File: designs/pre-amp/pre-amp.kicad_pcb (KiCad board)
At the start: 4 copper layers, 56.4 x 24.9 mm, 28 parts, among them J1 Conn_Coaxial, J2 Conn_01x03, J3 Conn_Coaxial, U1 AD8429, U2 OP211

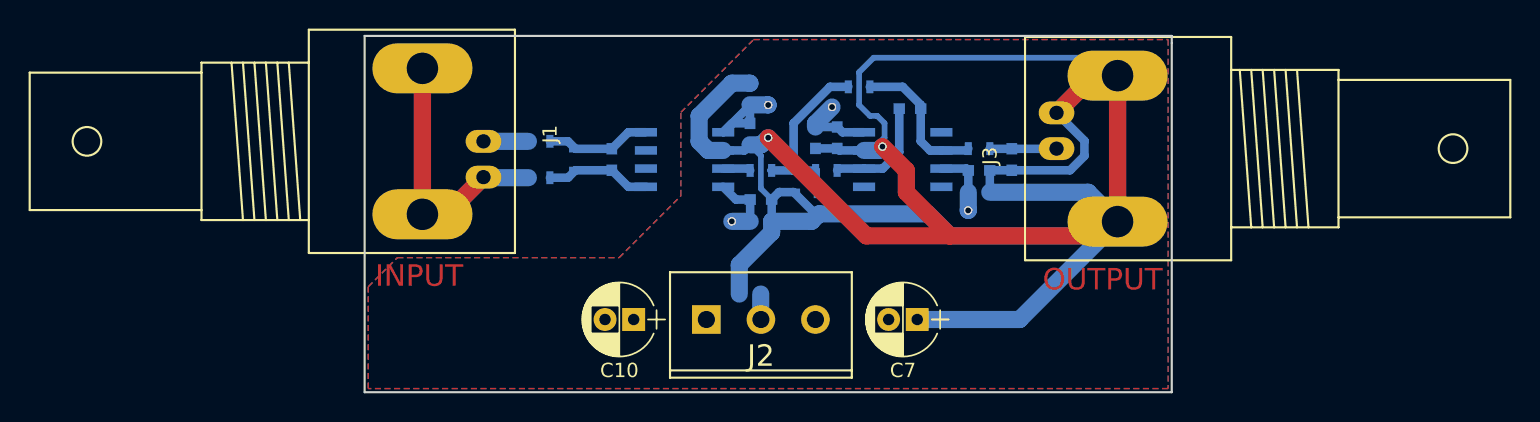
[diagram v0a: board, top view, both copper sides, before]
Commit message: [designs/pre-amp] new layout
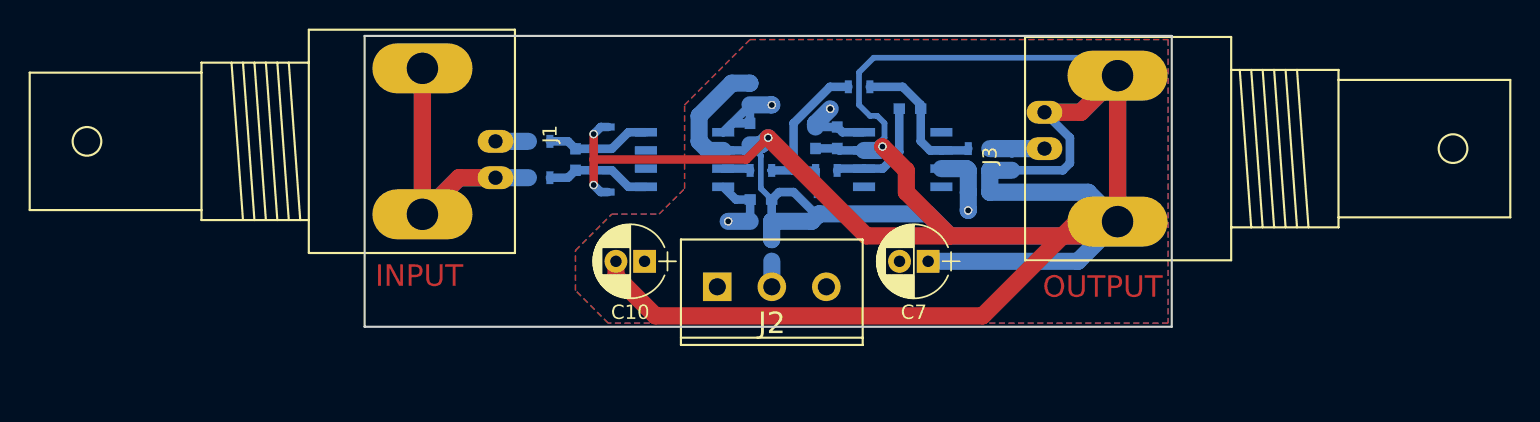
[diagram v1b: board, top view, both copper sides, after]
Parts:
- C14: value C -> 0
- J1, J3: footprint Connectors_TE-Connectivity:BNC_Socket_TYCO-AMP_LargePads -> Connectors2:BNC_Socket_Right-Angle_LargePads
- R4: value 20k -> 100k
- R8: value R -> 0
- R9: value R -> 100k
- moved R9 13.3 mm to (70.9, 64.5), turned to 270 degrees
- moved C10 4.13 mm to (73.4, 73.2)
- moved C7 4.13 mm to (93.2, 73.2)
- moved R3 3.41 mm to (82.3, 72.4), turned to 90 degrees
- moved R4 2.75 mm to (70.9, 67.6)
- moved C2 2.54 mm to (68.6, 66.0)
- moved J2 2.41 mm to (82.3, 74.9)
- moved J1 0.76 mm to (57.9, 64.8)
- moved J3 0.76 mm to (106.4, 65.3)
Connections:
- R4 pad 1: Net-(C2-Pad2) -> Net-(C2-Pad1)
- R4 pad 2: Net-(C2-Pad1) -> GND
- R9 pad 2: Net-(C12-Pad1) -> Net-(C2-Pad2)
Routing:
- net +15V: track 62.7 -> 52.7 mm
- net GND: track 238.4 -> 245.2 mm, vias 2 -> 4
- net -15V: track 52.9 -> 47.1 mm
- net Net-(J2-Pad2): track 3.91 -> 1.79 mm
- net Net-(J1-Pad1): track 3.14 -> 2.30 mm
- net Net-(C14-Pad1): track 4.67 -> 3.87 mm
- net Net-(J1-Pad2): track 34.2 -> 35.0 mm
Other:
- board size 56.4 x 24.9 mm -> 56.4 x 20.3 mm

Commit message: [designs/pre-amp] flip input and tweak connection near the edges
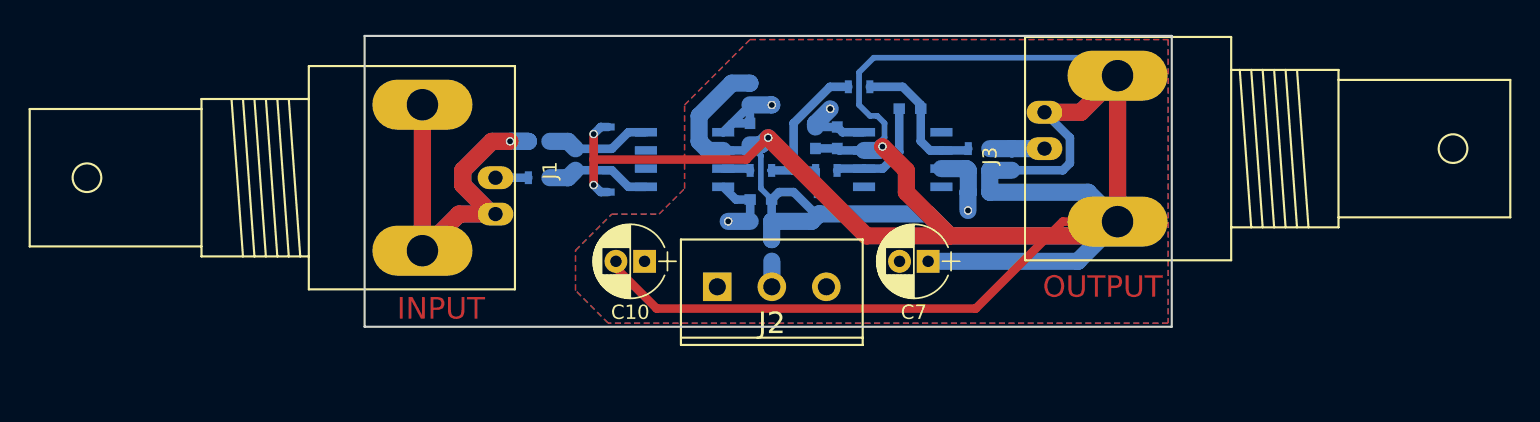
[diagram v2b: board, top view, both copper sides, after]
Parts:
- moved J1 2.54 mm to (57.9, 67.3)
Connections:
- R1 pad 2: Net-(J1-Pad2) -> Net-(J1-Pad1)
- R2 pad 2: Net-(J1-Pad1) -> Net-(J1-Pad2)
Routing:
- net +15V: track 52.7 -> 184.7 mm
- net Net-(J1-Pad2): track 35.0 -> 68.4 mm, vias 0 -> 1
- net GND: track 245.2 -> 247.3 mm
- net Net-(C2-Pad2): track 7.40 -> 9.41 mm
- net Net-(C2-Pad1): track 7.40 -> 9.41 mm

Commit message: [designs/pre-amp] move label location and update values
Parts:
- C2: value 0.02u -> 2200p
- R1, R2: value 1k -> 1.01k
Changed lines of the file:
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@@
     (links 55)
     (no_connects 0)
-    (area 30.174519 55.43586 134.163481 79.269001)
+    (area 53.772999 57.328999 110.311001 77.799001)
     (thickness 1.6)
-    (drawings 6)
+    (drawings 8)
     (tracks 252)
     (zones 0)
@@
     (nets 19)
   )
-  (page A4)
+  (page USLetter)
   (layers
     (0 F.Cu signal)
@@
   )
   (setup
-    (last_trace_width 1.2)
+    (last_trace_width 0.6)
     (user_trace_width 0.4)
     (user_trace_width 1.2)
@@
     (tags "capacitor 0603")
     (attr smd)
-    (fp_text reference C1 (at 0 1.5 270) (layer B.SilkS)
-      (effects (font (size 1 1) (thickness 0.15)) (justify mirror))
+    (fp_text reference C1 (at -0.182 -1.208 270) (layer B.SilkS)
+      (effects (font (size 0.762 0.762) (thickness 0.127)) (justify mirror))
     )
     (fp_text value 0.1u (at 0 -1.5 270) (layer B.Fab)
@@
     (tags "capacitor 0603")
     (attr smd)
-    (fp_text reference C2 (at 0 1.5 90) (layer B.SilkS)
-      (effects (font (size 1 1) (thickness 0.15)) (justify mirror))
-    )
-    (fp_text value 0.02u (at 0 -1.5 90) (layer B.Fab)
+    (fp_text reference C2 (at -2.38 0.08 90) (layer B.SilkS)
+      (effects (font (size 1 1) (thickness 0.15)) (justify mirror))
+    )
+    (fp_text value 2200p (at 0 -1.5 90) (layer B.Fab)
       (effects (font (size 1 1) (thickness 0.15)) (justify mirror))
     )
@@
     (tags "capacitor 0603")
     (attr smd)
-    (fp_text reference C3 (at 0 1.5 90) (layer B.SilkS)
+    (fp_text reference C3 (at 2.338 0.098 90) (layer B.SilkS)
       (effects (font (size 1 1) (thickness 0.15)) (justify mirror))
     )
@@
     (tags "capacitor 0603")
     (attr smd)
-    (fp_text reference C4 (at 0 1.5) (layer B.SilkS)
+    (fp_text reference C4 (at -2.424 0.726) (layer B.SilkS)
       (effects (font (size 1 1) (thickness 0.15)) (justify mirror))
     )
@@
     (tags "capacitor 0603")
     (attr smd)
-    (fp_text reference C6 (at 0 1.5 270) (layer B.SilkS)
-      (effects (font (size 1 1) (thickness 0.15)) (justify mirror))
+    (fp_text reference C6 (at -1.826 -0.032 360) (layer B.SilkS)
+      (effects (font (size 0.762 0.762) (thickness 0.127)) (justify mirror))
     )
     (fp_text value 0.1u (at 0 -1.5 270) (layer B.Fab)
@@
     (tags "capacitor 0603")
     (attr smd)
-    (fp_text reference C8 (at 0 1.5 270) (layer B.SilkS)
-      (effects (font (size 1 1) (thickness 0.15)) (justify mirror))
+    (fp_text reference C8 (at 0.004 1.164 270) (layer B.SilkS)
+      (effects (font (size 0.762 0.762) (thickness 0.127)) (justify mirror))
     )
     (fp_text value 10u (at 0 -1.5 270) (layer B.Fab)
@@
     (tags "capacitor 0603")
     (attr smd)
-    (fp_text reference C11 (at 0 1.5) (layer B.SilkS)
+    (fp_text reference C11 (at -2.814 0.822) (layer B.SilkS)
       (effects (font (size 1 1) (thickness 0.15)) (justify mirror))
     )
@@
     (tags "capacitor 0603")
     (attr smd)
-    (fp_text reference C12 (at 0 1.5 270) (layer B.SilkS)
-      (effects (font (size 1 1) (thickness 0.15)) (justify mirror))
+    (fp_text reference C12 (at 0.012 1.218 270) (layer B.SilkS)
+      (effects (font (size 0.762 0.762) (thickness 0.127)) (justify mirror))
     )
     (fp_text value C (at 0 -1.5 270) (layer B.Fab)
@@
     (tags "capacitor 0603")
     (attr smd)
-    (fp_text reference C14 (at 0 1.5 270) (layer B.SilkS)
-      (effects (font (size 1 1) (thickness 0.15)) (justify mirror))
+    (fp_text reference C14 (at 1.33 -1.17 270) (layer B.SilkS)
+      (effects (font (size 0.762 0.762) (thickness 0.127)) (justify mirror))
     )
     (fp_text value 0 (at 0 -1.5 270) (layer B.Fab)
@@
     (tags "resistor 0603")
     (attr smd)
-    (fp_text reference R1 (at 0 1.9 180) (layer B.SilkS)
-      (effects (font (size 1 1) (thickness 0.15)) (justify mirror))
-    )
-    (fp_text value 1k (at 0 -1.9 180) (layer B.Fab)
+    (fp_text reference R1 (at 0.01 -1.58 180) (layer B.SilkS)
+      (effects (font (size 1 1) (thickness 0.15)) (justify mirror))
+    )
+    (fp_text value 1.01k (at 0 -1.9 180) (layer B.Fab)
       (effects (font (size 1 1) (thickness 0.15)) (justify mirror))
     )
@@
       (effects (font (size 1 1) (thickness 0.15)) (justify mirror))
     )
-    (fp_text value 1k (at 0 -1.9 180) (layer B.Fab)
+    (fp_text value 1.01k (at 0 -1.9 180) (layer B.Fab)
       (effects (font (size 1 1) (thickness 0.15)) (justify mirror))
     )
@@
     (tags "resistor 0603")
     (attr smd)
-    (fp_text reference R4 (at 0 1.9 270) (layer B.SilkS)
+    (fp_text reference R4 (at 2.246 -0.094 270) (layer B.SilkS)
       (effects (font (size 1 1) (thickness 0.15)) (justify mirror))
     )
@@
     (tags "resistor 0603")
     (attr smd)
-    (fp_text reference R5 (at 0 1.9 180) (layer B.SilkS)
-      (effects (font (size 1 1) (thickness 0.15)) (justify mirror))
+    (fp_text reference R5 (at -1.846 0.182 270) (layer B.SilkS)
+      (effects (font (size 0.762 0.762) (thickness 0.127)) (justify mirror))
     )
     (fp_text value R (at 0 -1.9 180) (layer B.Fab)
@@
     (tags "resistor 0603")
     (attr smd)
-    (fp_text reference R7 (at 0 1.9 180) (layer B.SilkS)
-      (effects (font (size 1 1) (thickness 0.15)) (justify mirror))
+    (fp_text reference R7 (at 1.746 -0.508 270) (layer B.SilkS)
+      (effects (font (size 0.762 0.762) (thickness 0.127)) (justify mirror))
     )
     (fp_text value R (at 0 -1.9 180) (layer B.Fab)
@@
     (tags "resistor 0603")
     (attr smd)
-    (fp_text reference R9 (at 0 1.9 270) (layer B.SilkS)
+    (fp_text reference R9 (at -2.346 -0.064 270) (layer B.SilkS)
       (effects (font (size 1 1) (thickness 0.15)) (justify mirror))
     )
@@
     )
   )
+  (gr_circle (center 90.48 67.88) (end 90.88 68.07) (layer B.SilkS) (width 0.2))
+  (gr_circle (center 75.15 67.92) (end 75.58 68.04) (layer B.SilkS) (width 0.2))
   (gr_line (start 53.848 77.724) (end 53.848 57.404) (angle 90) (layer Edge.Cuts) (width 0.15))
   (gr_line (start 110.236 77.724) (end 53.848 77.724) (angle 90) (layer Edge.Cuts) (width 0.15))
